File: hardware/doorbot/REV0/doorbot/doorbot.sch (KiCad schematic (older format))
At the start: 41 parts, among them J1 Raspberry_Pi_2_3, J2 Screw_Terminal_01x12, J3 PoE Passthrough, Q1 2N7002, U1 ATmega328P-AU, U2 TLP291, U3 TLP291, U4 TLP291, U5 TLP291, U6 TLP291, U7 DRV103, U8 MC78L05_SOT89

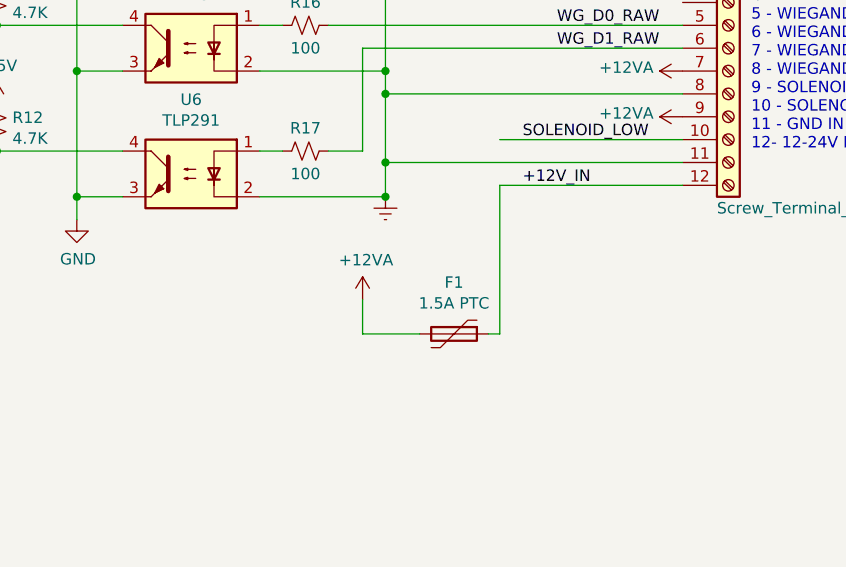
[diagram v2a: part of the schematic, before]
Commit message: doorbot: add dc boost for 24v option, PTC fuse
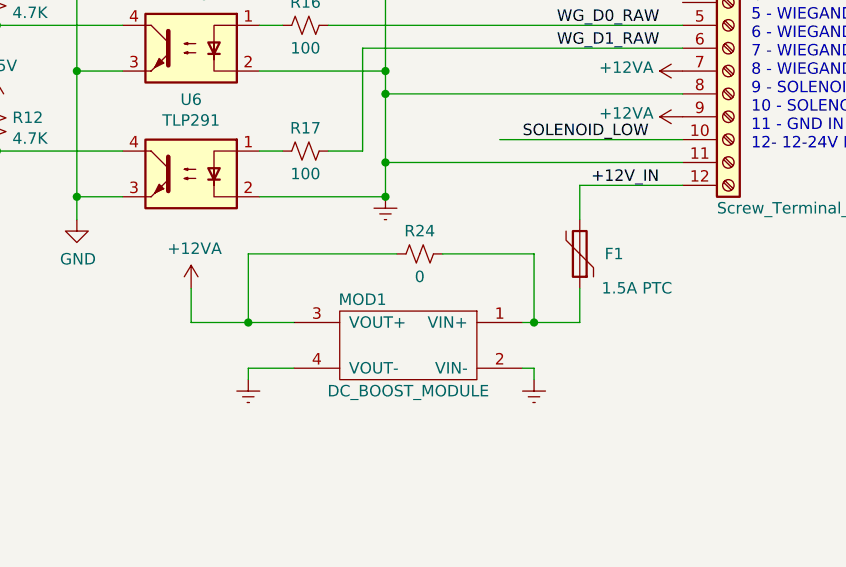
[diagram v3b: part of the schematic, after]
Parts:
- added MOD1: DC_BOOST_MODULE, doorbot_pcb_library:DC_BOOST_MODULE, symbol doorbot:DC_BOOST_MODULE
- added R24: 0, Resistors_SMD:R_0805, symbol Device:R_Small_US
- F1: footprint (none) -> Fuse_Holders_and_Fuses:Fuse_SMD1206_Reflow
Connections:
- wire segments 146 -> 157
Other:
- moved on the sheet: F1
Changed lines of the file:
@@
 Wire Wire Line
 	9800 5350 9000 5350
-Wire Wire Line
-	9800 5550 9000 5550
 $Comp
 L power:+12VA #PWR020
 U 1 1 5C9409B0
-P 8400 6050
-F 0 "#PWR020" H 8400 5900 50  0001 C CNN
-F 1 "+12VA" H 8415 6223 50  0000 C CNN
-F 2 "" H 8400 6050 50  0001 C CNN
-F 3 "" H 8400 6050 50  0001 C CNN
-	1    8400 6050
+P 7650 6000
+F 0 "#PWR020" H 7650 5850 50  0001 C CNN
+F 1 "+12VA" H 7665 6173 50  0000 C CNN
+F 2 "" H 7650 6000 50  0001 C CNN
+F 3 "" H 7650 6000 50  0001 C CNN
+	1    7650 6000
 	1    0    0    -1
 $EndComp
@@
 L Device:Polyfuse F1
 U 1 1 5C95A449
-P 8800 6200
-F 0 "F1" V 8575 6200 50  0000 C CNN
-F 1 "1.5A PTC" V 8666 6200 50  0000 C CNN
-F 2 "" H 8850 6000 50  0001 L CNN
-F 3 "~" H 8800 6200 50  0001 C CNN
-	1    8800 6200
-	0    1    1    0
-$EndComp
-Wire Wire Line
-	8650 6200 8400 6200
-Wire Wire Line
-	8400 6200 8400 6050
-Wire Wire Line
-	8950 6200 9000 6200
-Wire Wire Line
-	9000 6200 9000 5550
-Text Label 9100 5550 0    50   ~ 0
+P 9350 5850
+F 0 "F1" H 9200 5850 50  0000 C CNN
+F 1 "1.5A PTC" H 9100 6000 50  0000 C CNN
+F 2 "Fuse_Holders_and_Fuses:Fuse_SMD1206_Reflow" H 9400 5650 50  0001 L CNN
+F 3 "~" H 9350 5850 50  0001 C CNN
+	1    9350 5850
+	-1   0    0    1
+$EndComp
+Wire Wire Line
+	7900 6150 7650 6150
+Wire Wire Line
+	7650 6150 7650 6000
+Text Label 9400 5550 0    50   ~ 0
 +12V_IN
 $Comp
@@
 Wire Wire Line
 	4450 2200 2900 2200
+$Comp
+L doorbot:DC_BOOST_MODULE MOD1
+U 1 1 5C9167F2
+P 8900 6100
+F 0 "MOD1" H 9400 6150 50  0000 C CNN
+F 1 "DC_BOOST_MODULE" H 9200 5750 50  0000 C CNN
+F 2 "doorbot_pcb_library:DC_BOOST_MODULE" H 8900 6100 50  0001 C CNN
+F 3 "" H 8900 6100 50  0001 C CNN
+	1    8900 6100
+	-1   0    0    -1
+$EndComp
+Wire Wire Line
+	9350 5700 9350 5550
+Wire Wire Line
+	9350 5550 9800 5550
+$Comp
+L Device:R_Small_US R24
+U 1 1 5C934A88
+P 8650 5850
+F 0 "R24" V 8550 5850 50  0000 C CNN
+F 1 "0" V 8750 5850 50  0000 C CNN
+F 2 "Resistors_SMD:R_0805" H 8650 5850 50  0001 C CNN
+F 3 "~" H 8650 5850 50  0001 C CNN
+	1    8650 5850
+	0    1    1    0
+$EndComp
+Wire Wire Line
+	9100 6150 9150 6150
+Wire Wire Line
+	9350 6150 9350 6000
+Wire Wire Line
+	8750 5850 9150 5850
+Wire Wire Line
+	9150 5850 9150 6150
+Connection ~ 9150 6150
+Wire Wire Line
+	9150 6150 9350 6150
+Wire Wire Line
+	8550 5850 7900 5850
+Wire Wire Line
+	7900 5850 7900 6150
+Wire Wire Line
+	7900 6150 8100 6150
+$Comp
+L power:Earth #PWR0101
+U 1 1 5C94B070
+P 7900 6400
+F 0 "#PWR0101" H 7900 6150 50  0001 C CNN
+F 1 "Earth" H 7900 6250 50  0001 C CNN
+F 2 "" H 7900 6400 50  0001 C CNN
+F 3 "~" H 7900 6400 50  0001 C CNN
+	1    7900 6400
+	1    0    0    -1
+$EndComp
+$Comp
+L power:Earth #PWR0102
+U 1 1 5C94C66F
+P 9150 6400
+F 0 "#PWR0102" H 9150 6150 50  0001 C CNN
+F 1 "Earth" H 9150 6250 50  0001 C CNN
+F 2 "" H 9150 6400 50  0001 C CNN
+F 3 "~" H 9150 6400 50  0001 C CNN
+	1    9150 6400
+	1    0    0    -1
+$EndComp
+Wire Wire Line
+	9100 6350 9150 6350
+Wire Wire Line
+	9150 6350 9150 6400
+Wire Wire Line
+	7900 6400 7900 6350
+Wire Wire Line
+	7900 6350 8100 6350
+Connection ~ 7900 6150
 $EndSCHEMATC

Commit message: more doorbot schematic & pcb, routed and passes drc but not complete
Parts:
- added C5, C6: .1uF, Capacitor_SMD:C_0603_1608Metric, symbol Device:C_Small
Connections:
- net labels added: +VSW
- wire segments 157 -> 164
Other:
- moved on the sheet: C3, C4, U8

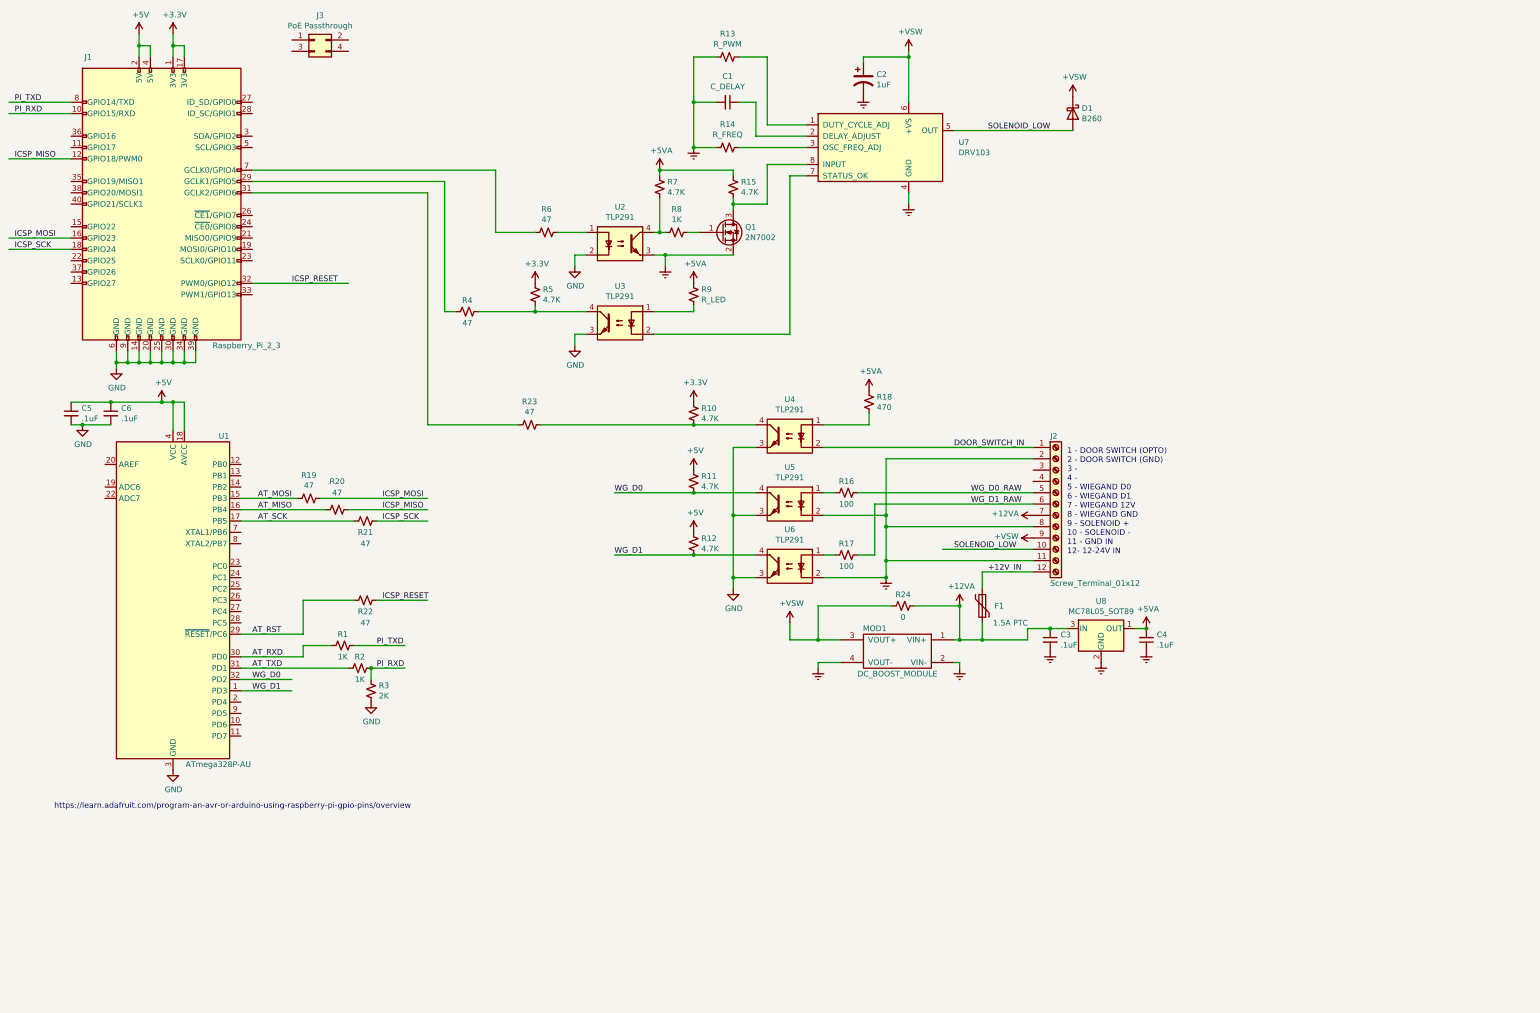
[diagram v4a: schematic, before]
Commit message: add wiegand led/buzzer control, leds, some rerouting
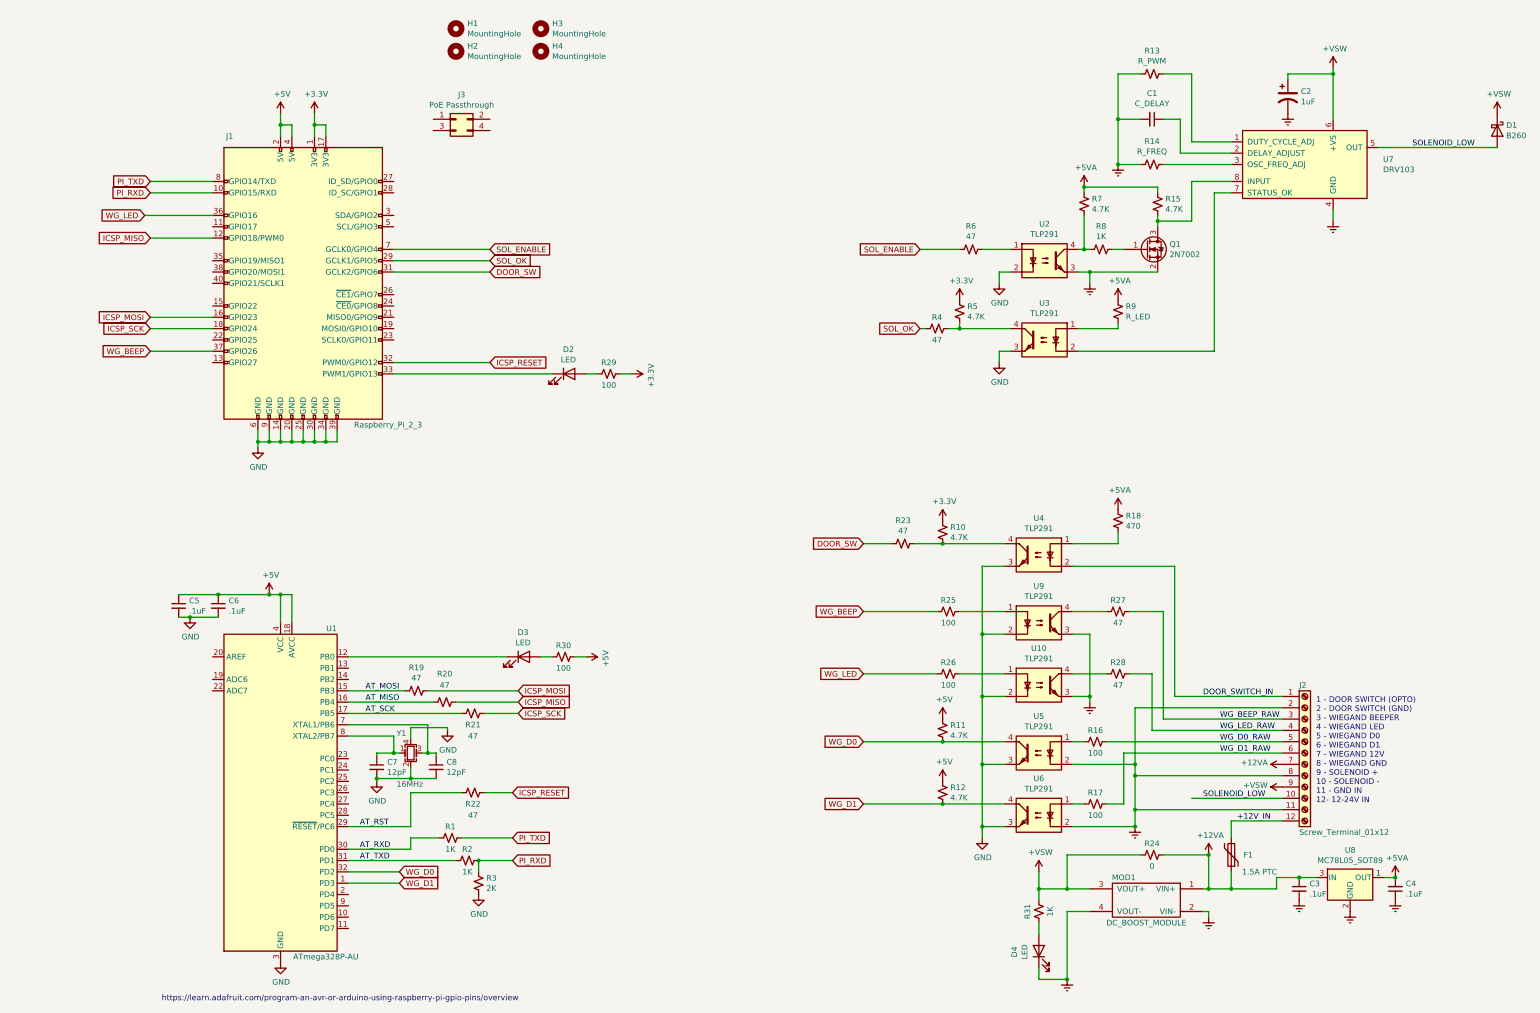
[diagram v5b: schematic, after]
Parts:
- added C7, C8: 12pF, Capacitors_SMD:C_0603, symbol Device:C_Small
- added D2, D3, D4: LED, LEDs:LED_0603_HandSoldering, symbol Device:LED
- added H1, H2, H3, H4: MountingHole, Mounting_Holes:MountingHole_2.7mm_M2.5, symbol Mechanical:MountingHole
- added R25, R26, R29, R30: 100, Resistors_SMD:R_0603, symbol Device:R_Small_US
- added R27, R28: 47, Resistors_SMD:R_0603, symbol Device:R_Small_US
- added R31: 1K, Resistors_SMD:R_0603, symbol Device:R_Small_US
- added U10, U9: TLP291, Housings_SOIC:SO-4_4.4x2.3mm_Pitch1.27mm, symbol Isolator:TLP291
- added Y1: 16MHz, Crystals:Crystal_SMD_2520-4pin_2.5x2.0mm, symbol Device:Crystal_GND24_Small
- J1: footprint Connector_PinHeader_2.54mm:PinHeader_2x20_P2.54mm_Vertical -> Pin_Headers:Pin_Header_Straight_2x20_Pitch2.54mm
- J3: footprint Connector_PinHeader_2.54mm:PinHeader_2x02_P2.54mm_Vertical -> Pin_Headers:Pin_Header_Straight_2x02_Pitch2.54mm
- R1, R10, R11, R12, R13, R14, R15, R16, R17, R18, R19, R2, R20, R21, R22, R23, R3, R4, R5, R6, R7, R8, R9: footprint Resistor_SMD:R_0603_1608Metric -> Resistors_SMD:R_0603
- U2, U3, U4, U5, U6: footprint Package_SO:SOIC-4_4.55x2.6mm_P1.27mm -> Housings_SOIC:SO-4_4.4x2.3mm_Pitch1.27mm
- U7: footprint Package_SO:SOIC-8_3.9x4.9mm_P1.27mm -> Housings_SOIC:SOIC-8_3.9x4.9mm_Pitch1.27mm
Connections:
- net labels added: DOOR_SW, SOL_ENABLE, SOL_OK, WG_BEEP, WG_BEEP_RAW, WG_LED, WG_LED_RAW
- wire segments 164 -> 212
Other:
- note added: "1 - DOOR SWITCH (OPTO)\n2 - DOOR SWITCH (GND)\n3 - WIEGAND BEEPER\n4 - WIEGAND LED\n5 - WIEGAND D0\n6 - WIEGAND D1\n7 - WIEGAND 12V\n8 - WIEGAND GND\n9 - SOLENOID +\n10 - SOLENOID -\n11 - GND IN\n12- 12-24V IN"
- note removed: "1 - DOOR SWITCH (OPTO)\n2 - DOOR SWITCH (GND)\n3 - \n4 - \n5 - WIEGAND D0\n6 - WIEGAND D1\n7 - WIEGAND 12V\n8 - WIEGAND GND\n9 - SOLENOID +\n10 - SOLENOID -\n11 - GND IN\n12- 12-24V IN"
- moved on the sheet: C1, C2, C3, C4, C5, C6, D1, F1, J1, J2, J3, MOD1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

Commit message: more doorbot pcb work
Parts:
- added C10: .1uF, Capacitors_SMD:C_0603, symbol Device:C_Small
- added C9: 1uF, Capacitors_SMD:CP_Elec_3x5.3, symbol Device:CP1
- added D5, D6, D7: BAT54S, TO_SOT_Packages_SMD:SOT-23, symbol Diode:BAT54S
- added J4: Conn_01x03, Pin_Headers:Pin_Header_Straight_1x03_Pitch2.54mm, symbol Connector_Generic:Conn_01x03
- added J5: Conn_01x04, Pin_Headers:Pin_Header_Straight_1x04_Pitch2.54mm, symbol Connector_Generic:Conn_01x04
- C3, C4, C5, C6: footprint Capacitor_SMD:C_0603_1608Metric -> Capacitors_SMD:C_0603
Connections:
- net +3V3: now also C10.1, D6.2, D7.2, J5.1 (Pin_1)
- net +5V: now also C9.1, D5.2, J4.1 (Pin_1)
- net GND: now also C10.2, C9.2, D5.1, D6.1, D7.1, J4.3 (Pin_3), J5.4 (Pin_4)
- net RGB_DATA: now reaches U1.23 (PC0)
- net RGB_DATA: now also D5.3, J4.2 (Pin_2)
- net at J1.3 (SDA/GPIO2): now also D6.3, J5.2 (Pin_2)
- net at J1.5 (SCL/GPIO3): now also D7.3, J5.3 (Pin_3)
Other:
- moved on the sheet: C3, C4, C7, C8, J3, R22, U8, Y1

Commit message: doorbot pcb rev0 draft 2 ready for review
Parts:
- removed J4: Conn_01x03, Pin_Headers:Pin_Header_Straight_1x03_Pitch2.54mm, symbol Connector_Generic:Conn_01x03
- added C11: 1uF, Capacitors_SMD:CP_Elec_3x5.3, symbol Device:CP1
- added C12: .1uF, Capacitors_SMD:C_0603, symbol Device:C_Small
- added D8: BAT54S, TO_SOT_Packages_SMD:SOT-23, symbol Diode:BAT54S
- added J4: Conn_01x04, Connect:Grove_1x04, symbol Connector_Generic:Conn_01x04
- added R32, R33: 4.7K, Resistors_SMD:R_0603, symbol Device:R_Small_US
- added RV1: 100K, Potentiometers:Potentiometer_Trimmer_Bourns_3269P, symbol Device:R_POT_US
- J5: footprint Pin_Headers:Pin_Header_Straight_1x04_Pitch2.54mm -> Connect:Grove_1x04
- renumbered D3 to LED1, D2 to LED2, D4 to LED3
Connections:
- net +3V3: now also J5.3 (Pin_3), C11.1; no longer J5.1 (Pin_1)
- net +5V: now also C12.1, D8.2, J4.3 (Pin_3), R32.1, R33.1
- net Earth: now also RV1.2
- net GND: now also C11.2, C12.2, D8.1, J4.4 (Pin_4)
- net AT_SDA: now reaches U1.27 (PC4)
- net AT_SDA: now also D8.3, J4.2 (Pin_2), R33.2
- net AT_SCL: now reaches U1.28 (PC5)
- net AT_SCL: now also D5.3, J4.1 (Pin_1), R32.2
- net PI_SDA: now reaches J1.3 (SDA/GPIO2), J5.2 (Pin_2)
- net PI_SDA: now also D7.3; no longer D6.3
- net at R13.1, U7.1 (DUTY_CYCLE_ADJ): now also RV1.1
- net RGB_DATA: no longer names the net of U1.23 (PC0)
- net RGB_DATA: no longer D5.3
- new net PI_SCL: D6.3, J1.5 (SCL/GPIO3), J5.1 (Pin_1)
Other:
- note added: "ATMEGA - GROVE DIGITAL or I2C\n1 - Yellow (primary digital I/O or SCL)\n2 - White (secondary digital I/O or SDA)\n3 - VCC (+5V)\n4 - GND"
- note added: "Atmega 328P"
- note added: "DELAY (Initial on @ 100% Duty) - Value of C1 (C_DELAY)\n====================================\n1µs ... Pin 2 Tied to +5V\n18µs ... Pin 2 Open\n110µs ... 100pF\n1.1ms ... 1nF\n11ms ... 10nF\n110ms ... 100nF\n1.1s ... 1µF ***\n11s ... 10µF"
- note added: "Isolated I/O & Power Supply"
- note added: "Isolated PWM Solenoid Driver"
- note added: "Misc."
- note added: "PI - GROVE DIGITAL or I2C - 3.3V ONLY!\n1 - Yellow (primary digital I/O or SCL)\n2 - White (secondary digital I/O or SDA)\n3 - VCC (+3.3V)\n4 - GND"
- note added: "PWM DUTY CYCLE (at 100kHz) - Value of R13 (R_PWM)\n==================================\n5% 16.9k\n10% 19.1k\n20% 22.6k\n30% 26.1k\n40% 29.4k\n50% 33.2k\n60% 37.4k\n70% 40.2k\n80% 44.2k\n90% 47.5k\n95% 49.9k\n\n"
- note added: "PWM FREQ - Value of R14 (R_FREQ)\n=======================\n100kHz ... 47.5k ***\n50kHz ... 100k\n25kHz ... 205k\n10kHz ... 523k\n5kHz ... 1.07M\n500Hz ... 11.3M"
- note added: "Raspberry Pi 3 Model B+"
- moved on the sheet: C1, C10, C2, C3, C4, C9, D1, D5, F1, H1, H2, H3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

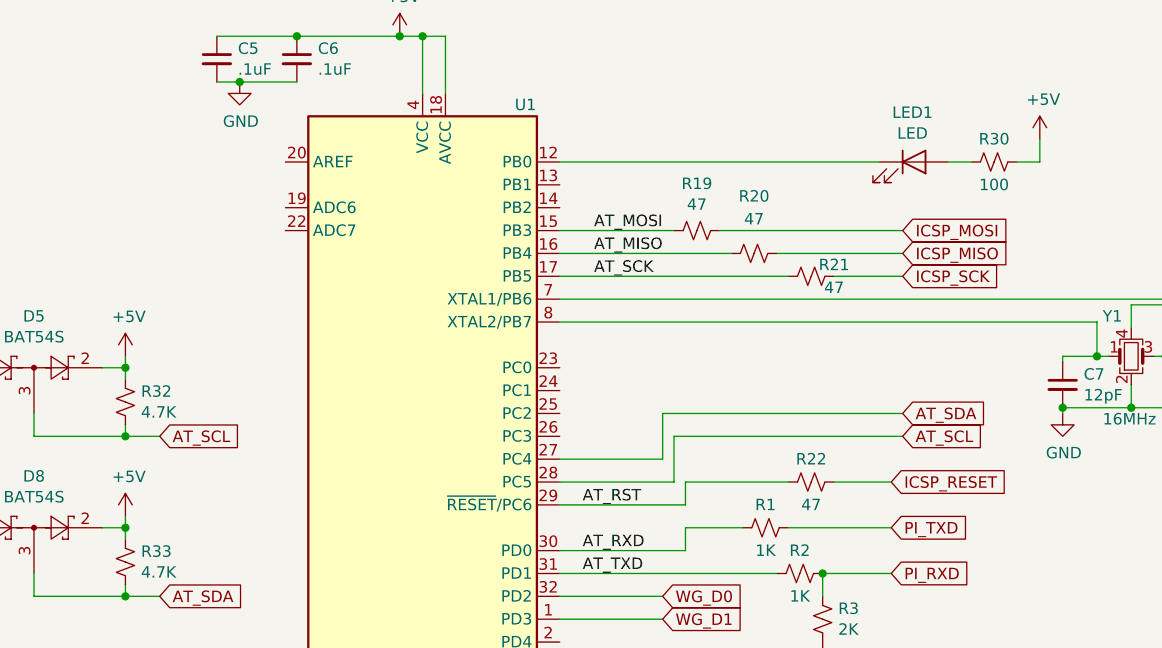
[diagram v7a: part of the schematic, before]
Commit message: add atmega reset pullup & AREF cap, fix footprint library issue, small tweaks & cleanup, ready for fab
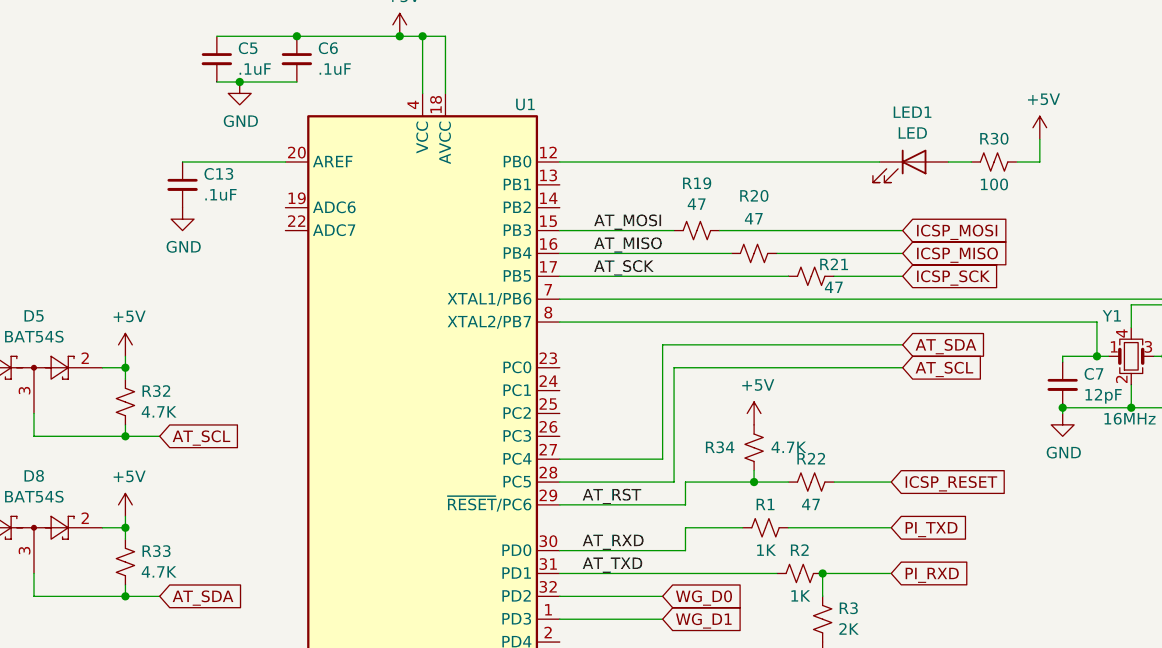
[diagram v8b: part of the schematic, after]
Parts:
- added C13: .1uF, Capacitor_SMD:C_0603_1608Metric, symbol Device:C_Small
- added R34: 4.7K, Resistor_SMD:R_0603_1608Metric, symbol Device:R_Small_US
- C10, C12, C3, C4, C5, C6, C7, C8: footprint Capacitors_SMD:C_0603 -> Capacitor_SMD:C_0603_1608Metric
- C11, C2, C9: footprint Capacitors_SMD:CP_Elec_3x5.3 -> Capacitor_SMD:CP_Elec_3x5.3
- D5, D6, D7, D8: footprint TO_SOT_Packages_SMD:SOT-23 -> Package_TO_SOT_SMD:SOT-23
- F1: footprint Fuse_Holders_and_Fuses:Fuse_SMD1206_Reflow -> Fuse:Fuse_1206_3216Metric_Pad1.42x1.75mm_HandSolder
- LED1, LED2, LED3: footprint LEDs:LED_0603_HandSoldering -> LED_SMD:LED_0603_1608Metric_Pad1.05x0.95mm_HandSolder
- R1, R10, R11, R12, R13, R14, R15, R16, R17, R18, R19, R2, R20, R21, R22, R23, R25, R26, R27, R28, R29, R3, R30, R31, R32, R33, R4, R5, R6, R7, R8, R9: footprint Resistors_SMD:R_0603 -> Resistor_SMD:R_0603_1608Metric
- R24: footprint Resistors_SMD:R_0805 -> Resistor_SMD:R_0603_1608Metric
- U10, U2, U3, U4, U5, U6, U9: footprint Housings_SOIC:SO-4_4.4x2.3mm_Pitch1.27mm -> Package_SO:SO-4_4.4x2.3mm_P1.27mm
- Y1: footprint Crystals:Crystal_SMD_2520-4pin_2.5x2.0mm -> Crystal:Crystal_SMD_2520-4Pin_2.5x2.0mm
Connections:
- net +5V: now also R34.1
- net AT_RST: now also R34.2
- net GND: now also C13.2
- net at U1.20 (AREF): now also C13.1
